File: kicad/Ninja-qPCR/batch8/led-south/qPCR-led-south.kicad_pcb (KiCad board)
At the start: 2 copper layers, 115.5 x 16.4 mm, 10 parts, among them U1 Conn_02x05

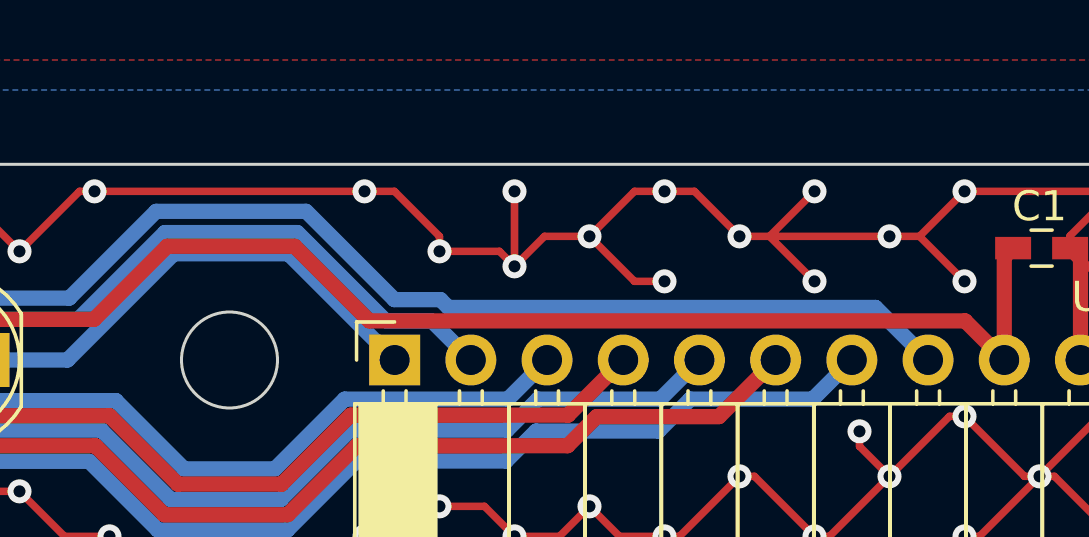
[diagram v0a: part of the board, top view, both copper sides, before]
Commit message: ordered batch8 and got feedback
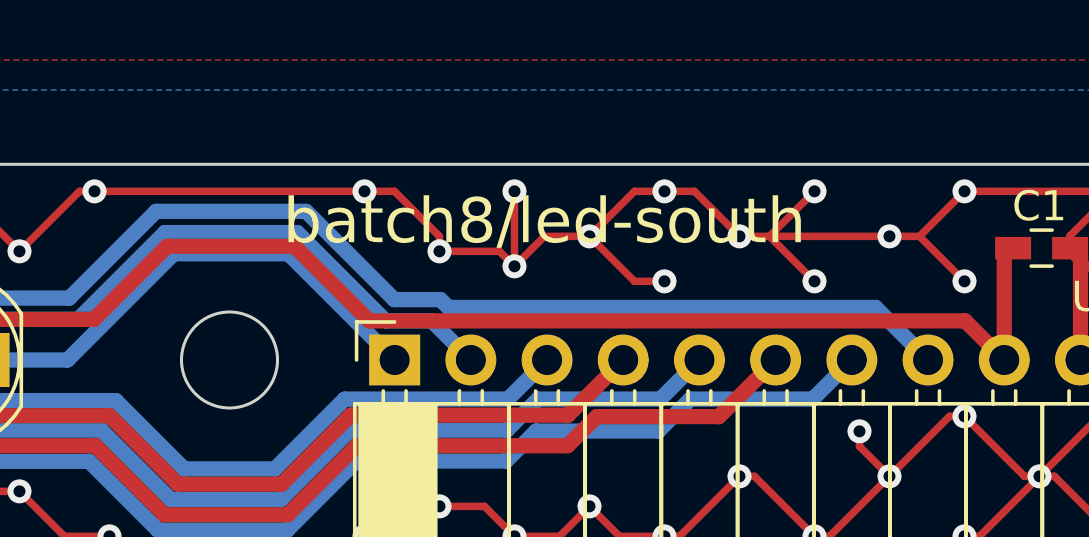
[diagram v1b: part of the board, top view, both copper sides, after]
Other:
- board text added: "batch8/led-south"
